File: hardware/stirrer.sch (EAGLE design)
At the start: 53 parts, among them Q2 FDN306P, Q3 8 MHz, U1 PIC24FV16KM202, U2 A4960, U3 PIC24FV32KA302, X1 ICD, X2 Console

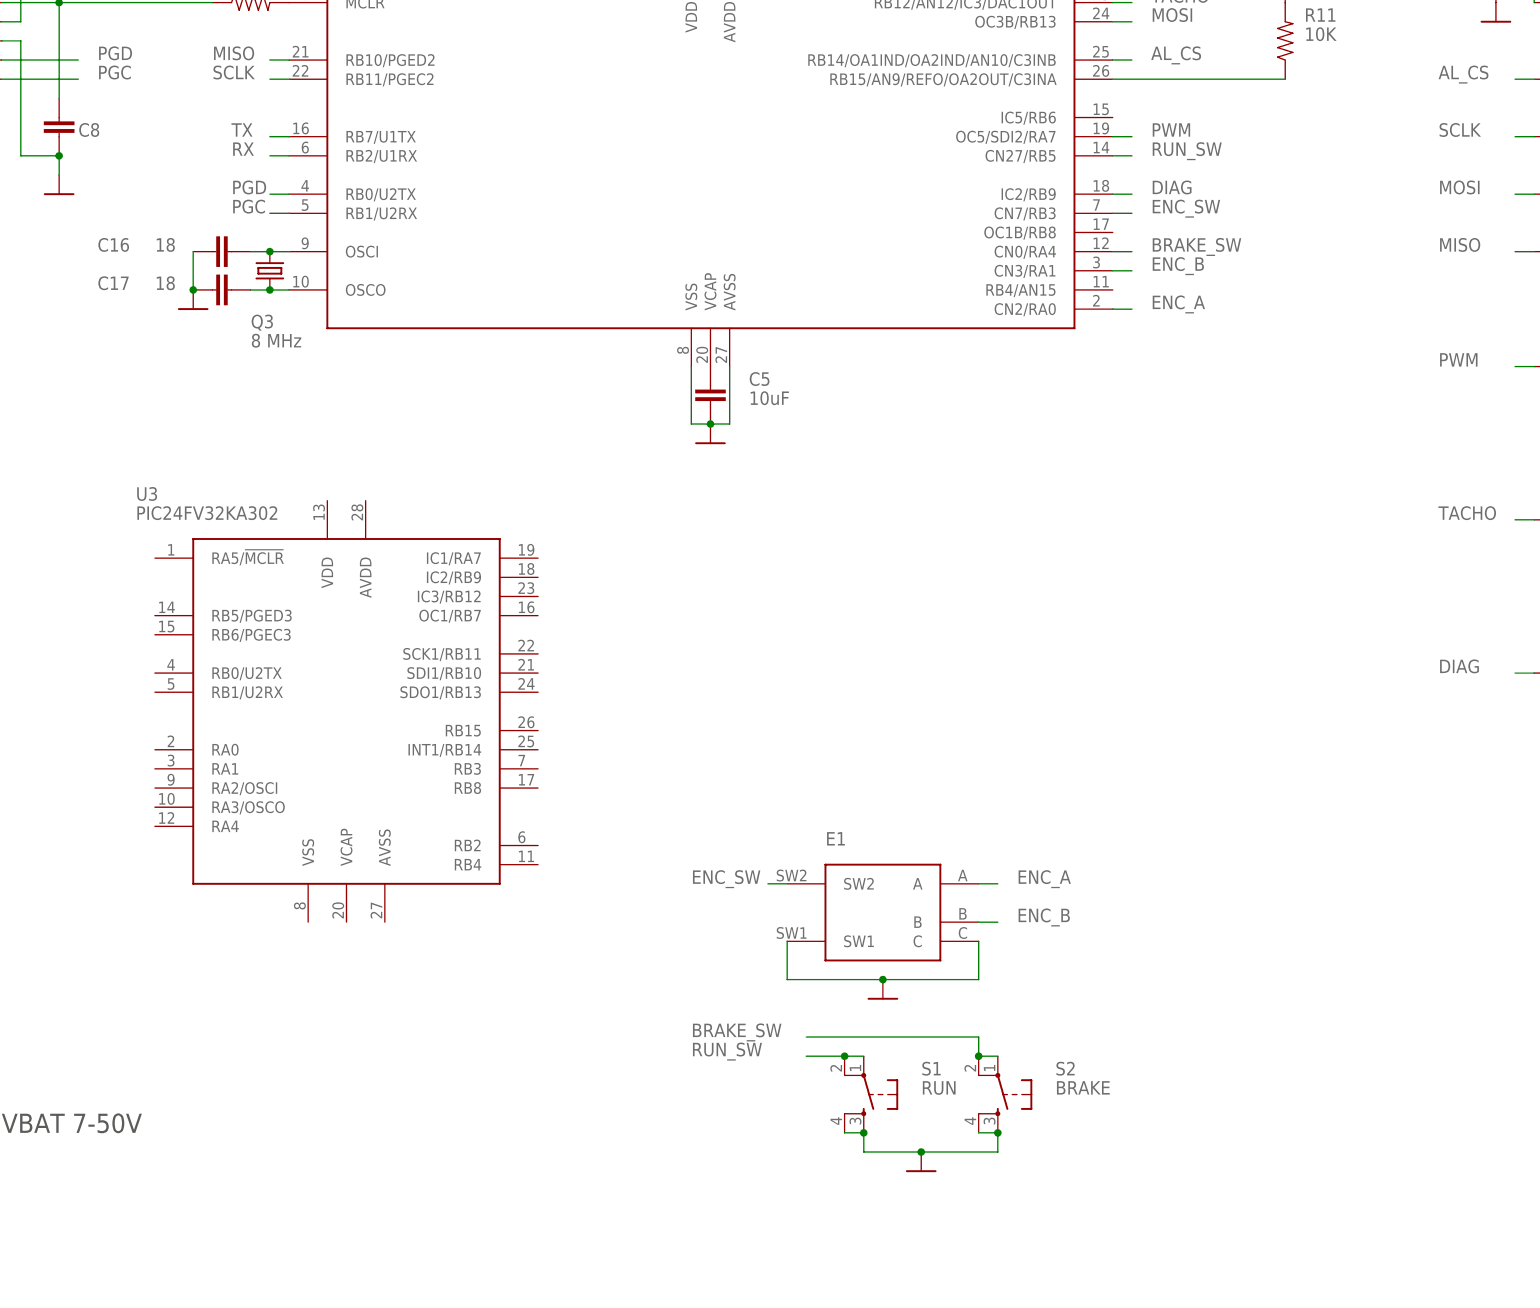
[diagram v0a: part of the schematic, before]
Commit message: initial layout of display compartment
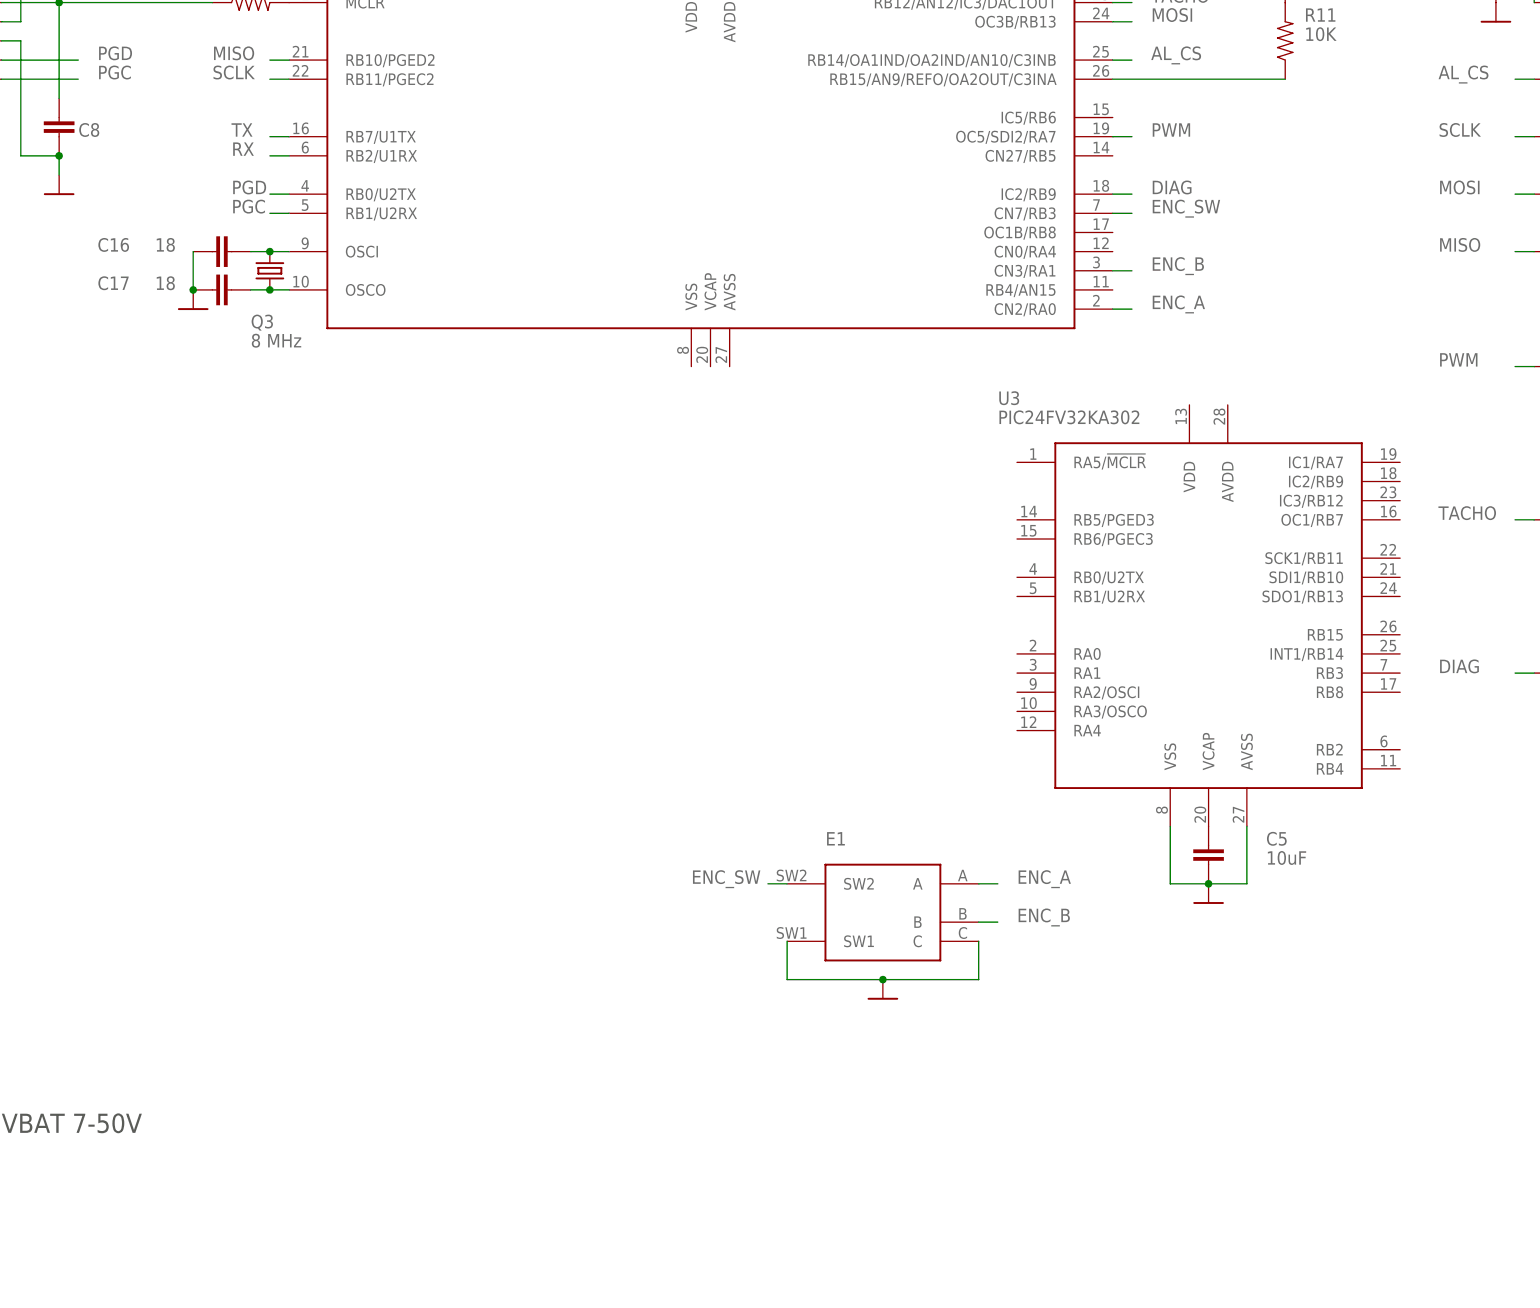
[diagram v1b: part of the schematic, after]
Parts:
- removed S1: RUN, ch_passive:TAC_SWITCHPTH
- removed S2: BRAKE, ch_passive:TAC_SWITCHPTH
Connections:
- removed net BRAKE_SW: S2.1, S2.2, U1.CN0/RA4
- removed net RUN_SW: S1.1, S1.2, U1.CN27/RB5
- net GND: now also U3.AVSS, U3.VSS; no longer S1.3, S1.4, S2.3, S2.4, U1.AVSS, U1.VSS
- net N$1: now also U3.VCAP; no longer U1.VCAP
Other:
- moved on the sheet: C5, U3
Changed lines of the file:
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@@
 <part name="P+3" library="ch_passive" deviceset="+5V" device=""/>
 <part name="GND7" library="ch_passive" deviceset="GND" device=""/>
-<part name="S1" library="ch_passive" deviceset="TAC_SWITCH" device="PTH" value="RUN"/>
-<part name="GND9" library="ch_passive" deviceset="GND" device=""/>
-<part name="S2" library="ch_passive" deviceset="TAC_SWITCH" device="PTH" value="BRAKE"/>
 <part name="U2" library="ch_allegro" deviceset="A4960" device="" value="A4960"/>
 <part name="C9" library="ch_passive" deviceset="C" device="-0603" value="470n"/>
@@
 <attribute name="NAME" x="134.62" y="228.6" size="1.778" layer="95"/>
 </instance>
-<instance part="C5" gate="G$1" x="142.24" y="165.1" smashed="yes">
-<attribute name="NAME" x="147.32" y="165.1" size="1.778" layer="95"/>
-<attribute name="VALUE" x="147.32" y="162.56" size="1.778" layer="96"/>
-</instance>
-<instance part="GND2" gate="1" x="142.24" y="157.48" smashed="yes"/>
+<instance part="C5" gate="G$1" x="208.28" y="104.14" smashed="yes">
+<attribute name="NAME" x="215.9" y="104.14" size="1.778" layer="95"/>
+<attribute name="VALUE" x="215.9" y="101.6" size="1.778" layer="96"/>
+</instance>
+<instance part="GND2" gate="1" x="208.28" y="96.52" smashed="yes"/>
 <instance part="GND3" gate="1" x="152.4" y="223.52" smashed="yes"/>
 <instance part="GND4" gate="1" x="132.08" y="223.52" smashed="yes"/>
@@
 </instance>
 <instance part="GND7" gate="1" x="30.48" y="180.34" smashed="yes"/>
-<instance part="S1" gate="S" x="162.56" y="71.12" smashed="yes" rot="R270">
-<attribute name="NAME" x="170.18" y="73.66" size="1.778" layer="95"/>
-<attribute name="VALUE" x="170.18" y="71.12" size="1.778" layer="96"/>
-</instance>
-<instance part="GND9" gate="1" x="170.18" y="60.96" smashed="yes"/>
-<instance part="S2" gate="S" x="180.34" y="71.12" smashed="yes" rot="R270">
-<attribute name="NAME" x="187.96" y="73.66" size="1.778" layer="95"/>
-<attribute name="VALUE" x="187.96" y="71.12" size="1.778" layer="96"/>
-</instance>
 <instance part="U2" gate="G$1" x="276.86" y="185.42" smashed="yes">
 <attribute name="NAME" x="269.24" y="215.9" size="1.778" layer="95"/>
@@
 <attribute name="VALUE" x="218.44" y="228.6" size="1.778" layer="96"/>
 </instance>
-<instance part="U3" gate="G$1" x="96.52" y="121.92" smashed="yes">
-<attribute name="NAME" x="66.04" y="149.86" size="1.778" layer="95"/>
-<attribute name="VALUE" x="66.04" y="147.32" size="1.778" layer="96"/>
+<instance part="U3" gate="G$1" x="210.82" y="134.62" smashed="yes">
+<attribute name="NAME" x="180.34" y="162.56" size="1.778" layer="95"/>
+<attribute name="VALUE" x="180.34" y="160.02" size="1.778" layer="96"/>
 </instance>
 </instances>
@@
 </segment>
 <segment>
-<pinref part="C5" gate="G$1" pin="2"/>
-<pinref part="GND2" gate="1" pin="GND"/>
-<pinref part="U1" gate="G$1" pin="AVSS"/>
-<wire x1="144.78" y1="167.64" x2="144.78" y2="160.02" width="0.1524" layer="91"/>
-<wire x1="144.78" y1="160.02" x2="142.24" y2="160.02" width="0.1524" layer="91"/>
-<junction x="142.24" y="160.02"/>
-<pinref part="U1" gate="G$1" pin="VSS"/>
-<wire x1="139.7" y1="167.64" x2="139.7" y2="160.02" width="0.1524" layer="91"/>
-<wire x1="139.7" y1="160.02" x2="142.24" y2="160.02" width="0.1524" layer="91"/>
-</segment>
-<segment>
 <pinref part="C3" gate="G$1" pin="2"/>
 <pinref part="GND3" gate="1" pin="GND"/>
@@
 <pinref part="GND7" gate="1" pin="GND"/>
 <wire x1="30.48" y1="182.88" x2="30.48" y2="185.42" width="0.1524" layer="91"/>
-</segment>
-<segment>
-<pinref part="S1" gate="S" pin="3"/>
-<pinref part="GND9" gate="1" pin="GND"/>
-<wire x1="162.56" y1="66.04" x2="162.56" y2="63.5" width="0.1524" layer="91"/>
-<wire x1="162.56" y1="63.5" x2="170.18" y2="63.5" width="0.1524" layer="91"/>
-<wire x1="170.18" y1="63.5" x2="180.34" y2="63.5" width="0.1524" layer="91"/>
-<junction x="170.18" y="63.5"/>
-<pinref part="S2" gate="S" pin="3"/>
-<wire x1="180.34" y1="63.5" x2="180.34" y2="66.04" width="0.1524" layer="91"/>
-<pinref part="S2" gate="S" pin="4"/>
-<wire x1="180.34" y1="66.04" x2="177.8" y2="66.04" width="0.1524" layer="91"/>
-<junction x="180.34" y="66.04"/>
-<pinref part="S1" gate="S" pin="4"/>
-<wire x1="160.02" y1="66.04" x2="162.56" y2="66.04" width="0.1524" layer="91"/>
-<junction x="162.56" y="66.04"/>
 </segment>
 <segment>
@@
 <wire x1="55.88" y1="193.04" x2="55.88" y2="195.58" width="0.1524" layer="91"/>
 <junction x="55.88" y="195.58"/>
+</segment>
+<segment>
+<pinref part="C5" gate="G$1" pin="2"/>
+<pinref part="GND2" gate="1" pin="GND"/>
+<pinref part="U3" gate="G$1" pin="VSS"/>
+<wire x1="203.2" y1="106.68" x2="203.2" y2="99.06" width="0.1524" layer="91"/>
+<wire x1="203.2" y1="99.06" x2="208.28" y2="99.06" width="0.1524" layer="91"/>
+<junction x="208.28" y="99.06"/>
+<pinref part="U3" gate="G$1" pin="AVSS"/>
+<wire x1="213.36" y1="106.68" x2="213.36" y2="99.06" width="0.1524" layer="91"/>
+<wire x1="213.36" y1="99.06" x2="208.28" y2="99.06" width="0.1524" layer="91"/>
 </segment>
 </net>
@@
 </segment>
 </net>
-<net name="N$1" class="0">
-<segment>
-<pinref part="U1" gate="G$1" pin="VCAP"/>
-<pinref part="C5" gate="G$1" pin="1"/>
-</segment>
-</net>
 <net name="PWM" class="0">
 <segment>
@@
 </segment>
 </net>
-<net name="RUN_SW" class="0">
-<segment>
-<pinref part="S1" gate="S" pin="1"/>
-<pinref part="S1" gate="S" pin="2"/>
-<wire x1="162.56" y1="76.2" x2="160.02" y2="76.2" width="0.1524" layer="91"/>
-<wire x1="154.94" y1="76.2" x2="160.02" y2="76.2" width="0.1524" layer="91"/>
-<junction x="160.02" y="76.2"/>
-<label x="139.7" y="76.2" size="1.778" layer="95"/>
-</segment>
-<segment>
-<pinref part="U1" gate="G$1" pin="CN27/RB5"/>
-<wire x1="198.12" y1="195.58" x2="195.58" y2="195.58" width="0.1524" layer="91"/>
-<label x="200.66" y="195.58" size="1.778" layer="95"/>
-</segment>
-</net>
-<net name="BRAKE_SW" class="0">
-<segment>
-<pinref part="S2" gate="S" pin="1"/>
-<pinref part="S2" gate="S" pin="2"/>
-<wire x1="180.34" y1="76.2" x2="177.8" y2="76.2" width="0.1524" layer="91"/>
-<wire x1="154.94" y1="78.74" x2="177.8" y2="78.74" width="0.1524" layer="91"/>
-<wire x1="177.8" y1="78.74" x2="177.8" y2="76.2" width="0.1524" layer="91"/>
-<junction x="177.8" y="76.2"/>
-<label x="139.7" y="78.74" size="1.778" layer="95"/>
-</segment>
-<segment>
-<pinref part="U1" gate="G$1" pin="CN0/RA4"/>
-<wire x1="198.12" y1="182.88" x2="195.58" y2="182.88" width="0.1524" layer="91"/>
-<label x="200.66" y="182.88" size="1.778" layer="95"/>
-</segment>
-</net>
 <net name="N$9" class="0">
 <segment>
@@
 </segment>
 </net>
+<net name="N$1" class="0">
+<segment>
+<pinref part="U3" gate="G$1" pin="VCAP"/>
+<pinref part="C5" gate="G$1" pin="1"/>
+</segment>
+</net>
